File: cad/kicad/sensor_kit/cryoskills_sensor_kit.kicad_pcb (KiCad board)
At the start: 2 copper layers, 150 x 60 mm, 58 parts, among them J1 PWR_In, J10 QWIIC_I2C_2, J12 DS18B20, J13 Conn_01x02, J14 PT1000_RTD_WHEAT, J2 PWR_SENSE_Panel, J3 PWR_SENSE_Battery, J4 Conn_01x02, J5 Conn_01x02, J6 Conn_01x02, J7 PT1000_RTD_CC, J8 SPI_BREAKOUT, J9 QWIIC_I2C_1, SW1 SPDT Switch, U1 LM317_TO-220, U2 RFM96W, U3 INA3221, U4 LM334Z, U5 LM234Z-3

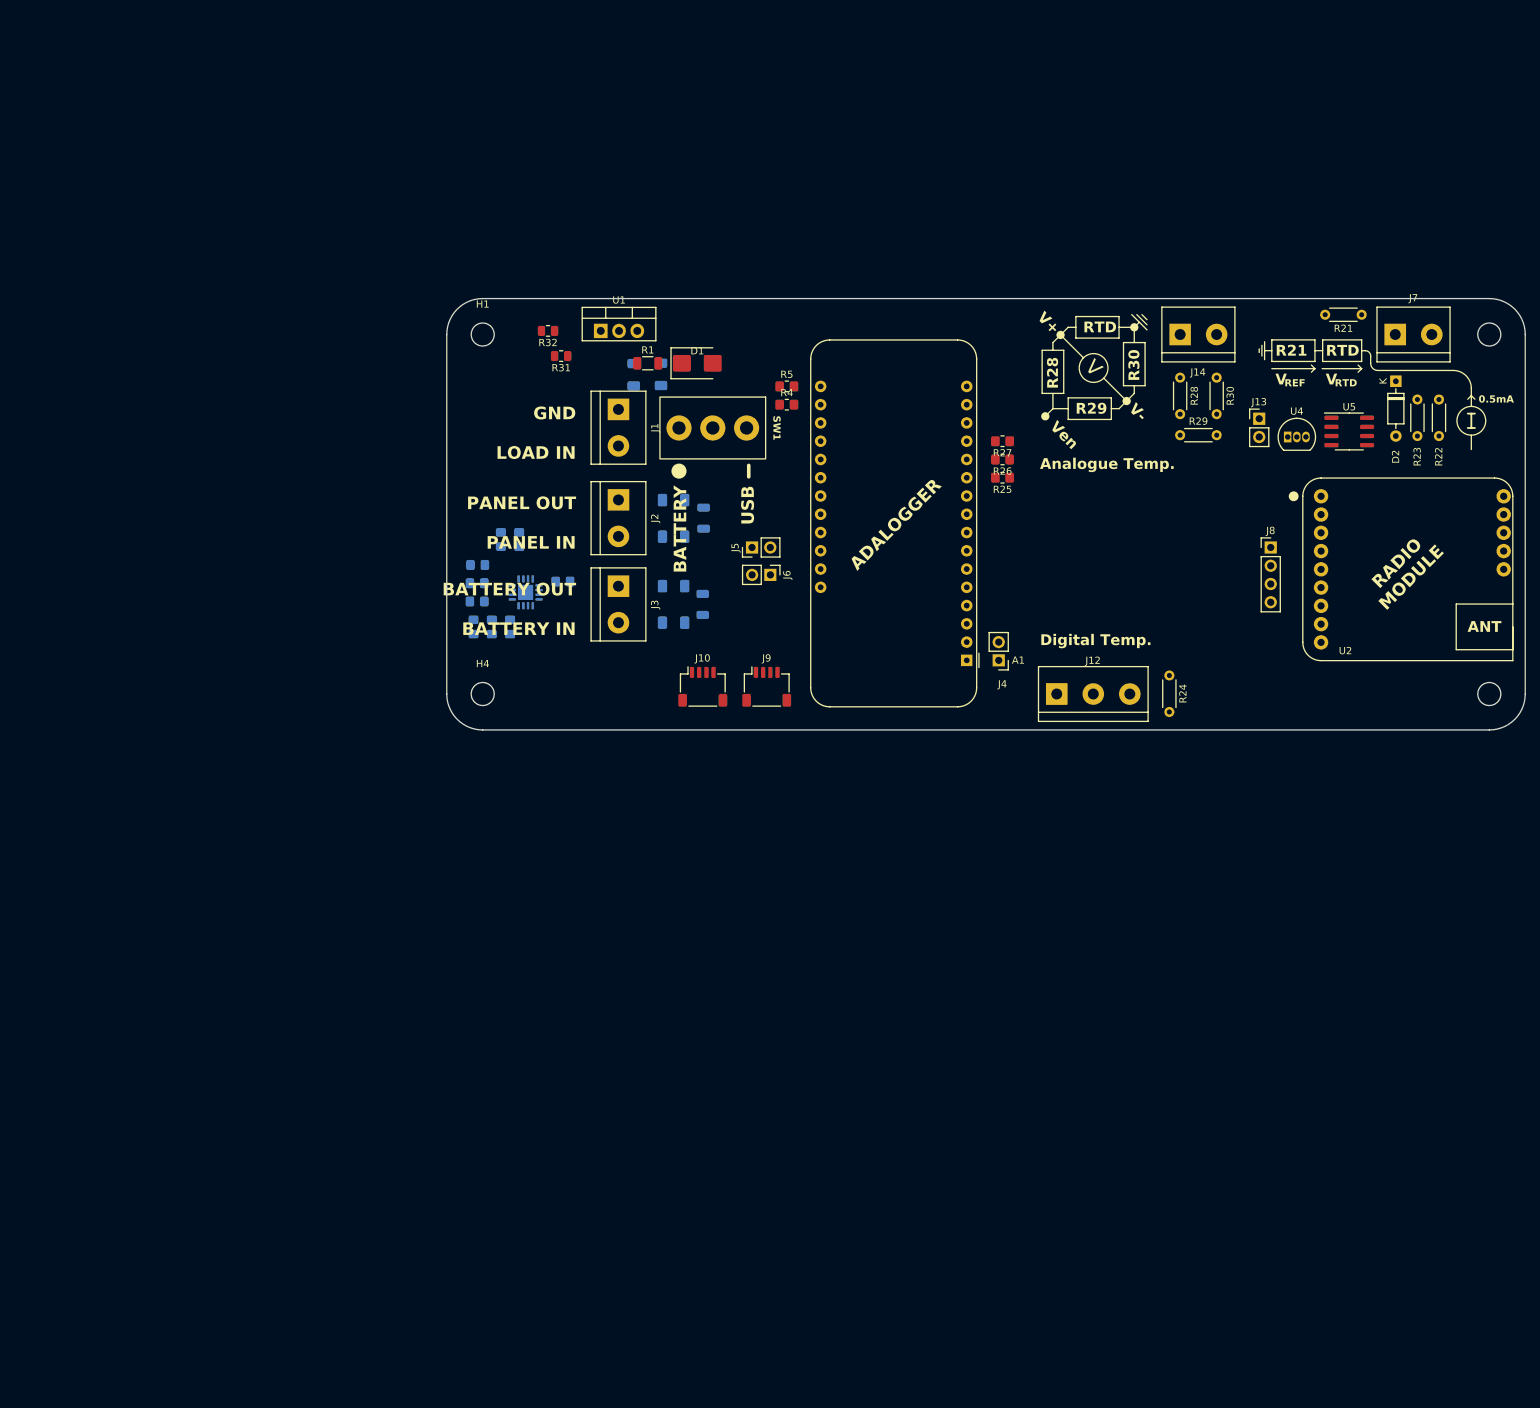
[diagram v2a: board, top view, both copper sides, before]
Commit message: revises sensor board to remove current source and reduce footprint
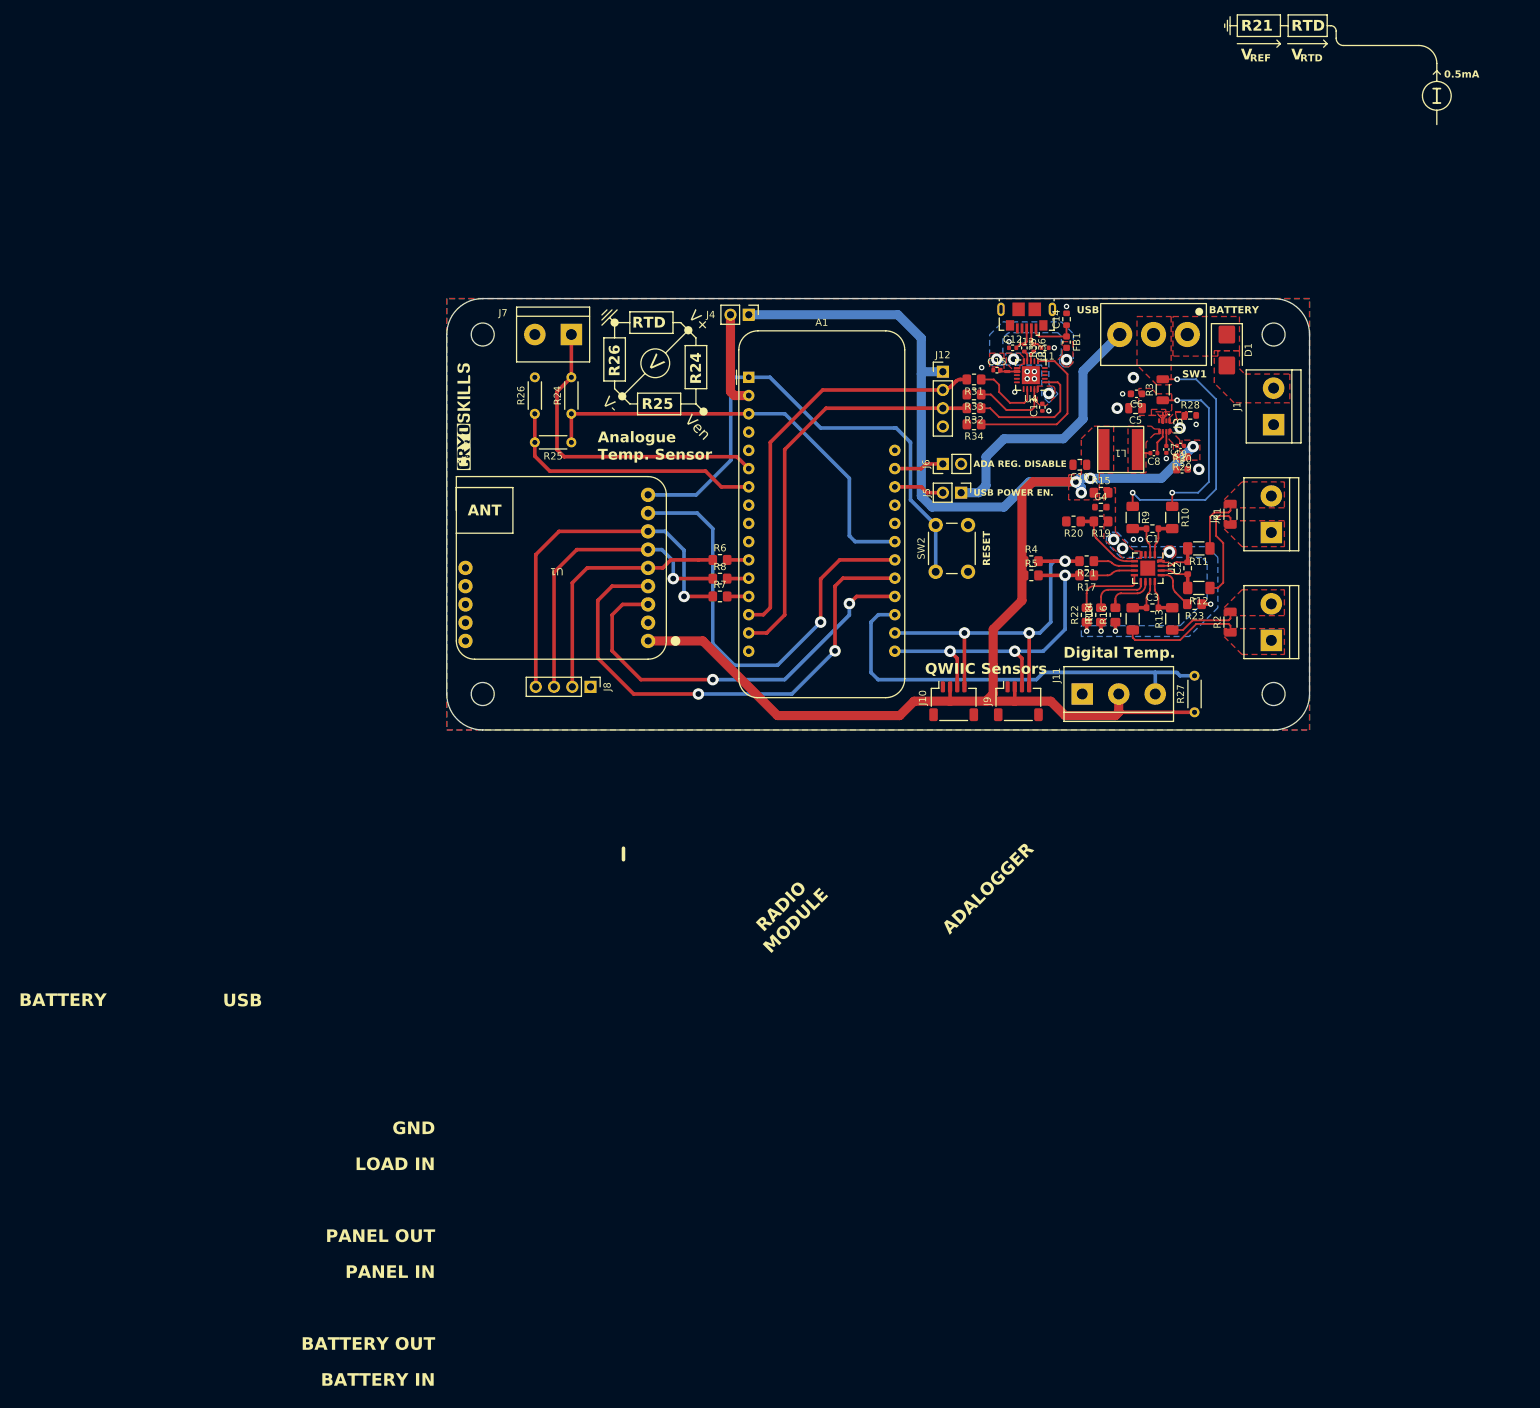
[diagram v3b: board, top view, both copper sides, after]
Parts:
- removed D2: 1N4149, Diode_THT:D_DO-35_SOD27_P7.62mm_Horizontal
- removed J14: PT1000_RTD_WHEAT, cryoskills_sensor_kit:TerminalBlock_Multicomp_5.08_2way_MP012059
- removed U5: LM234Z-3, Package_SO:SOIC-8_3.9x4.9mm_P1.27mm
- added C1: 0.1 uF, Resistor_SMD:R_0603_1608Metric, F.Cu at (156.7, 104.0)
- added C10: 100nF, Capacitor_SMD:C_0805_2012Metric, F.Cu at (146.6, 95.1)
- added C11: 47pF, Resistor_SMD:R_0402_1005Metric, F.Cu at (141.7, 78.8)
- added C12: 47pF, Resistor_SMD:R_0402_1005Metric, F.Cu at (137.2, 78.9)
- added C13: 100nF, Resistor_SMD:R_0402_1005Metric, F.Cu at (141.3, 87.1)
- added C14: 10nF, Resistor_SMD:R_0603_1608Metric, F.Cu at (144.7, 74.9)
- added C15: 100nF, Resistor_SMD:R_0402_1005Metric, F.Cu at (135.0, 82.0)
- added C2: 0.1 uF, Resistor_SMD:R_0603_1608Metric, F.Cu at (161.6, 109.5)
- added C3: 0.1 uF, Resistor_SMD:R_0603_1608Metric, F.Cu at (156.7, 115.0)
- added C4: 0.1 uF, Resistor_SMD:R_0603_1608Metric, F.Cu at (149.5, 101.0)
- added C5: 10uF, Capacitor_SMD:C_0805_2012Metric, F.Cu at (154.3, 87.2)
- added C6: 100nF, Capacitor_SMD:C_0603_1608Metric, F.Cu at (154.4, 85.2)
- added C7: 33nF, Capacitor_SMD:C_0402_1005Metric, F.Cu at (158.6, 93.0)
- added C8: 100nF, Capacitor_SMD:C_0402_1005Metric, F.Cu at (156.8, 93.5)
- added C9: 47pF, Capacitor_SMD:C_0402_1005Metric, F.Cu at (160.6, 92.5)
- added FB1: FerriteBead, Inductor_SMD:L_0603_1608Metric, F.Cu at (144.7, 78.1)
- added G***: LOGO, LOGO, F.Cu at (60.5, 88.5)
- added J11: DS18B20, cryoskills_sensor_kit:TerminalBlock_Multicomp_5.08_3way_MP012060, F.Cu at (146.9, 127.0)
- added L1: 2.7uH, cryoskills_sensor_kit:1255AY-2R7N#, F.Cu at (152.2, 93.0)
- added R33: 0R, Resistor_SMD:R_0805_2012Metric_Pad1.20x1.40mm_HandSolder, F.Cu at (131.8, 85.3)
- added R34: 0R, Resistor_SMD:R_0805_2012Metric_Pad1.20x1.40mm_HandSolder, F.Cu at (131.8, 89.5)
- added R35: 27R, Resistor_SMD:R_0402_1005Metric, F.Cu at (138.8, 78.9)
- added R36: 27R, Resistor_SMD:R_0402_1005Metric, F.Cu at (140.1, 78.8)
- added SW2: SW_Push, Button_Switch_THT:SW_PUSH_6mm, F.Cu at (126.5, 110.0)
- J12: value DS18B20 -> SERIAL_BREAKOUT; footprint cryoskills_sensor_kit:TerminalBlock_Multicomp_5.08_3way_MP012060 -> Connector_PinHeader_2.54mm:PinHeader_1x04_P2.54mm_Vertical
- J13: value Conn_01x02 -> USB_B; footprint Connector_PinHeader_2.54mm:PinHeader_1x02_P2.54mm_Vertical -> Connector_USB:USB_Micro-B_GCT_USB3076-30-A
- J4: value Conn_01x02 -> Adalogger_3V3
- J5: value Conn_01x02 -> Adalogger_VBUS
- J6: value Conn_01x02 -> Adalogger_RegulatorEN
- J7: value PT1000_RTD_CC -> PT1000_RTD_WHEAT
- R10, R11, R17, R2, R3, R9: moved to F.Cu
- R12, R14: value 0R -> 10 Ohm; footprint Resistor_SMD:R_0805_2012Metric_Pad1.20x1.40mm_HandSolder -> Resistor_SMD:R_1206_3216Metric_Pad1.30x1.75mm_HandSolder; moved to F.Cu
- R13: value 10k -> 10 Ohm; footprint Resistor_SMD:R_0805_2012Metric_Pad1.20x1.40mm_HandSolder -> Resistor_SMD:R_1206_3216Metric_Pad1.30x1.75mm_HandSolder; moved to F.Cu
- R15, R20: value 10k -> 0R; moved to F.Cu
- R16: value DNF -> 10k; moved to F.Cu
- R18: value 0R -> 10k; moved to F.Cu
- R19: value 10k -> DNF; moved to F.Cu
- R21: value 3k -> 0R; footprint Resistor_THT:R_Axial_DIN0204_L3.6mm_D1.6mm_P5.08mm_Horizontal -> Resistor_SMD:R_0805_2012Metric_Pad1.20x1.40mm_HandSolder
- R22: value 330R -> 10k; footprint Resistor_THT:R_Axial_DIN0204_L3.6mm_D1.6mm_P5.08mm_Horizontal -> Resistor_SMD:R_0805_2012Metric_Pad1.20x1.40mm_HandSolder
- R23: value 2.4k -> 10k; footprint Resistor_THT:R_Axial_DIN0204_L3.6mm_D1.6mm_P5.08mm_Horizontal -> Resistor_SMD:R_0805_2012Metric_Pad1.20x1.40mm_HandSolder
- R24: value 4.7k -> 3k3
- R25: value 0R -> 3k3; footprint Resistor_SMD:R_0805_2012Metric_Pad1.20x1.40mm_HandSolder -> Resistor_THT:R_Axial_DIN0204_L3.6mm_D1.6mm_P5.08mm_Horizontal
- R26: value 0R -> 1k; footprint Resistor_SMD:R_0805_2012Metric_Pad1.20x1.40mm_HandSolder -> Resistor_THT:R_Axial_DIN0204_L3.6mm_D1.6mm_P5.08mm_Horizontal
- R27: value 0R -> 4.7k; footprint Resistor_SMD:R_0805_2012Metric_Pad1.20x1.40mm_HandSolder -> Resistor_THT:R_Axial_DIN0204_L3.6mm_D1.6mm_P5.08mm_Horizontal
- R28: value 3k -> 15k; footprint Resistor_THT:R_Axial_DIN0204_L3.6mm_D1.6mm_P5.08mm_Horizontal -> Resistor_SMD:R_0603_1608Metric
- R29: value 3k -> 30.9k; footprint Resistor_THT:R_Axial_DIN0204_L3.6mm_D1.6mm_P5.08mm_Horizontal -> Capacitor_SMD:C_0603_1608Metric
- R30: value 1k -> 10k; footprint Resistor_THT:R_Axial_DIN0204_L3.6mm_D1.6mm_P5.08mm_Horizontal -> Capacitor_SMD:C_0603_1608Metric
- R31: value 1.2k -> 0R; footprint Resistor_SMD:R_0805_2012Metric -> Resistor_SMD:R_0805_2012Metric_Pad1.20x1.40mm_HandSolder
- R32: value 1.8k -> 0R; footprint Resistor_SMD:R_0805_2012Metric -> Resistor_SMD:R_0805_2012Metric_Pad1.20x1.40mm_HandSolder
- R6, R7, R8: value 10 Ohm -> 0R; footprint Resistor_SMD:R_1206_3216Metric_Pad1.30x1.75mm_HandSolder -> Resistor_SMD:R_0805_2012Metric_Pad1.20x1.40mm_HandSolder; moved to F.Cu
- U1: value LM317_TO-220 -> RFM96W; footprint Package_TO_SOT_THT:TO-220-3_Vertical -> cryoskills_sensor_kit:RFM96W
- U2: value RFM96W -> INA3221; footprint cryoskills_sensor_kit:RFM96W -> Package_DFN_QFN:Texas_RGV_S-PVQFN-N16_EP2.1x2.1mm
- U3: value INA3221 -> TPS62932DRLR; footprint Package_DFN_QFN:Texas_RGV_S-PVQFN-N16_EP2.1x2.1mm -> cryoskills_sensor_kit:TPS62932DRLR; moved to F.Cu
- U4: value LM334Z -> FT231XQ; footprint Package_TO_SOT_THT:TO-92_Inline -> Package_DFN_QFN:QFN-20-1EP_4x4mm_P0.5mm_EP2.5x2.5mm
- moved H3 148.7 mm to (63.5, 77.0)
- moved J7 114.6 mm to (75.8, 77.0), turned to 180 degrees
- moved H1 110.0 mm to (173.5, 77.0)
- moved J8 96.6 mm to (78.5, 126.0), turned to -90 degrees
- moved R12 96.0 mm to (163.1, 112.2), turned to 180 degrees
- moved U3 91.8 mm to (158.3, 89.7), turned to -90 degrees
- moved R13 91.5 mm to (159.4, 116.5), turned to 90 degrees
- moved R14 91.3 mm to (153.9, 116.5), turned to 90 degrees
- moved J1 91.1 mm to (173.5, 89.5), turned to 90 degrees
- moved J3 91.1 mm to (173.2, 119.5), turned to 90 degrees
- moved J2 90.9 mm to (173.2, 104.5), turned to 90 degrees
- moved R24 90.8 mm to (75.8, 88.0), turned to 90 degrees
- moved R19 86.9 mm to (149.5, 103.0)
- moved R18 86.8 mm to (149.5, 116.0), turned to 90 degrees
- moved R16 86.8 mm to (151.5, 116.0)
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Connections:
- net Net-(A1-3V3) renamed /VCC_3V3_Adalogger
- net Net-(A1-USB) renamed /VBUS_Adalogger
- A1 pad 21: /RADIO_CS -> /RADIO_IRQ
- A1 pad 22: /RADIO_IRQ -> /RADIO_CS
- A1 pad 23: /RTD_WHEAT_EN -> /ADC_REF+
- A1 pad 6: /ADC_RTD+ -> /ADC_RTDp
- A1 pad 7: /ADC_REF+ -> /ADC_RTDm
- D1 pad 1: /Isense_VCC_A -> Net-(D1-K)
- D1 pad 2: /V_IN -> /V_BAT
- J10 pad 3: /SCL -> /SDA
- J10 pad 4: /SDA -> /SCL
- J12 pad 1: GND -> /VCC_3V3
- J12 pad 2: /VCC_3V3 -> /UART_RXuC
- J12 pad 3: /DS18B20_DATA -> /UART_TXuC
- J13 pad 1: /VCC_3V3 -> Net-(J13-VBUS)
- J13 pad 2: /Sensors/CC_IN -> Net-(J13-D-)
- J7 pad 1: /ADC_RTD+ -> /ADC_RTDp
- J7 pad 2: /ADC_REF+ -> GND
- J9 pad 3: /SCL -> /SDA
- J9 pad 4: /SDA -> /SCL
- R1 pad 1: /Isense_VCC_B -> /Isense_Panel_B
- R1 pad 2: /Isense_VCC_A -> /Isense_Panel_A
- R10 pad 1: /Isense_Battery_A -> /Isense_VCC_B
- R10 pad 2: /Power Monitor/INA3221_IN+3 -> /Power Monitor/INA3221_INm3
- R11 pad 1: /Isense_Battery_B -> /Isense_Panel_A
- R11 pad 2: /Power Monitor/INA3221_IN-3 -> /Power Monitor/INA3221_INp2
- R12 pad 1: /VCC_3V3 -> /Isense_Panel_B
- R12 pad 2: /Power Monitor/VCC_INA3221 -> /Power Monitor/INA3221_INm2
- R13 pad 1: /Power Monitor/VCC_INA3221 -> /Isense_Battery_A
- R13 pad 2: unconnected-(R13-Pad2) -> /Power Monitor/INA3221_INp1
- R14 pad 1: Net-(U3-SDA) -> /Isense_Battery_B
- R14 pad 2: /SDA -> /Power Monitor/INA3221_INm1
- R15 pad 1: /Power Monitor/VCC_INA3221 -> /VCC_3V3
- R15 pad 2: unconnected-(R15-Pad2) -> /Power Monitor/VCC_INA3221
- R16 pad 2: /Power Monitor/INA3221_I2CAddress -> unconnected-(R16-Pad2)
- R17 pad 1: /Power Monitor/INA3221_I2CAddress -> Net-(U2-SDA)
- R17 pad 2: GND -> /SDA
- R18 pad 1: Net-(U3-SCL) -> /Power Monitor/VCC_INA3221
- R18 pad 2: /SCL -> unconnected-(R18-Pad2)
- R19 pad 2: unconnected-(R19-Pad2) -> /Power Monitor/INA3221_I2CAddress
- R2 pad 1: /Isense_Panel_B -> /Isense_Battery_B
- R2 pad 2: /Isense_Panel_A -> /Isense_Battery_A
- R20 pad 1: /Power Monitor/VCC_INA3221 -> /Power Monitor/INA3221_I2CAddress
- R20 pad 2: unconnected-(R20-Pad2) -> GND
- R21 pad 1: /ADC_REF+ -> Net-(U2-SCL)
- R21 pad 2: GND -> /SCL
- R22 pad 1: /Sensors/CC_ADJ -> /Power Monitor/VCC_INA3221
- R22 pad 2: /Sensors/CC_OUT -> unconnected-(R22-Pad2)
- R23 pad 1: /Sensors/CC_ADJ -> /Power Monitor/VCC_INA3221
- R23 pad 2: /ADC_RTD+ -> unconnected-(R23-Pad2)
- R24 pad 1: /VCC_3V3 -> /ADC_REF+
- R24 pad 2: /DS18B20_DATA -> /ADC_RTDp
- R25 pad 1: /SCK -> /ADC_REF+
- R25 pad 2: Net-(A1-SCK/D24) -> /ADC_RTDm
- R26 pad 1: /MOSI -> /ADC_RTDm
- R26 pad 2: Net-(A1-MOSI/D23) -> GND
- R27 pad 1: /MISO -> /VCC_3V3
- R27 pad 2: Net-(A1-MISO/D22) -> /DS18B20_DATA
- R28 pad 1: /ADC_REF+ -> Net-(U3-RT)
- R28 pad 2: /ADC_RTD+ -> GND
- R29 pad 1: /ADC_REF+ -> /VCC_3V3
- R29 pad 2: /ADC_REF+ -> Net-(U3-FB)
- R3 pad 1: /Isense_Battery_B -> /Isense_VCC_B
- R3 pad 2: /Isense_Battery_A -> /Isense_VCC_A
- R30 pad 1: /ADC_REF+ -> Net-(U3-FB)
- R31 pad 1: /VCC_3V3 -> Net-(U4-TXD)
- R31 pad 2: Net-(U1-ADJ) -> /UART_RXuC
- R32 pad 1: Net-(U1-ADJ) -> Net-(U4-RXD)
- R32 pad 2: GND -> /UART_TXuC
- R6 pad 1: /Isense_VCC_A -> /SCK
- R6 pad 2: /Power Monitor/INA3221_IN+1 -> Net-(A1-SCK/D24)
- R7 pad 1: /Isense_VCC_B -> /MISO
- R7 pad 2: /Power Monitor/INA3221_IN-1 -> Net-(A1-MISO/D22)
- R8 pad 1: /Isense_Panel_A -> /MOSI
- R8 pad 2: /Power Monitor/INA3221_IN+2 -> Net-(A1-MOSI/D23)
- R9 pad 1: /Isense_Panel_B -> /Isense_VCC_A
- R9 pad 2: /Power Monitor/INA3221_IN-2 -> /Power Monitor/INA3221_INp3
- SW1 pad 1: /V_BAT -> Net-(D1-K)
- SW1 pad 2: /V_IN -> /Isense_VCC_A
- U1 pad 1: Net-(U1-ADJ) -> /VCC_3V3
- U1 pad 2: /VCC_3V3 -> GND
- U1 pad 3: /Isense_VCC_B -> /RADIO_EN
- U2 pad 1: /VCC_3V3 -> /Power Monitor/INA3221_INm3
- U2 pad 10: unconnected-(U2-G5-Pad10) -> unconnected-(R16-Pad2)
- U2 pad 11: unconnected-(U2-G4-Pad11) -> /Power Monitor/INA3221_INm1
- U2 pad 12: unconnected-(U2-G3-Pad12) -> /Power Monitor/INA3221_INp1
- U2 pad 13: unconnected-(U2-G2-Pad13) -> unconnected-(R23-Pad2)
- U2 pad 14: unconnected-(U2-G1-Pad14) -> /Power Monitor/INA3221_INm2
- U2 pad 2: GND -> /Power Monitor/INA3221_INp3
- U2 pad 3: /RADIO_EN -> GND
- U2 pad 4: /RADIO_IRQ -> /Power Monitor/VCC_INA3221
- U2 pad 5: /SCK -> /Power Monitor/INA3221_I2CAddress
- U2 pad 6: /MOSI -> Net-(U2-SCL)
- U2 pad 7: /MISO -> Net-(U2-SDA)
- U2 pad 8: /RADIO_CS -> unconnected-(R22-Pad2)
- U2 pad 9: /~{RESET} -> unconnected-(R18-Pad2)
- U3 pad 1: /Power Monitor/INA3221_IN-3 -> Net-(U3-RT)
- U3 pad 2: /Power Monitor/INA3221_IN+3 -> unconnected-(U3-EN-Pad2)
- U3 pad 3: GND -> /Isense_VCC_B
- U3 pad 4: /Power Monitor/VCC_INA3221 -> GND
- U3 pad 5: /Power Monitor/INA3221_I2CAddress -> Net-(U3-SW)
- U3 pad 6: Net-(U3-SCL) -> Net-(U3-BST)
- U3 pad 7: Net-(U3-SDA) -> Net-(U3-SS)
- U3 pad 8: unconnected-(R19-Pad2) -> Net-(U3-FB)
- U4 pad 1: /Sensors/CC_IN -> Net-(U4-RXD)
- U4 pad 2: /Sensors/CC_ADJ -> unconnected-(U4-~{RI}-Pad2)
- U4 pad 3: /Sensors/CC_OUT -> GND
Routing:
- net /VCC_3V3: track 0.00 -> 224.3 mm, vias 0 -> 4
- net /~{RESET}: track 0.00 -> 73.1 mm
- net /RADIO_IRQ: track 0.00 -> 71.2 mm, vias 0 -> 2
- net /RADIO_CS: track 0.00 -> 62.0 mm, vias 0 -> 1
- net /ADC_REF+: track 0.00 -> 60.5 mm
- net /DS18B20_DATA: track 0.00 -> 59.8 mm
- net /RADIO_EN: track 0.00 -> 57.3 mm, vias 0 -> 2
- net /UART_RXuC: track 0.00 -> 57.2 mm
- net /UART_TXuC: track 0.00 -> 56.8 mm
- net /SCL: track 0.00 -> 53.3 mm, vias 0 -> 3
- net /MISO: track 0.00 -> 51.9 mm, vias 0 -> 1
- net /SDA: track 0.00 -> 48.9 mm, vias 0 -> 3
- net /ADC_RTDp: track 0.00 -> 44.6 mm
- net /MOSI: track 0.00 -> 42.4 mm, vias 0 -> 1
- net /V_BUS: track 0.00 -> 37.4 mm
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- added copper zone on F.Cu, net /Isense_Battery_A
- added copper zone on F.Cu, net /Isense_Battery_B
- added copper zone on F.Cu, net /Isense_Panel_A
- added copper zone on F.Cu, net /Isense_Panel_B
- added copper zone on F.Cu, net /Isense_VCC_A
- added copper zone on F.Cu, net /Isense_VCC_B
- added copper zone on B.Cu, net /Power Monitor/VCC_INA3221
- added copper zone on F.Cu, net /Power Monitor/VCC_INA3221
- added copper zone on F.Cu, net /VCC_3V3
- added copper zone on F.Cu, net /V_BAT
- added copper zone on B.Cu, net GND
- added copper zone on F.Cu, net GND
- added copper zone on F.Cu, net Net-(D1-K)
- added copper zone on F.Cu, net Net-(U3-FB)
- added copper zone on F.Cu, net Net-(U3-RT)
- added copper zone on F.Cu, net Net-(U3-SW)
- added copper zone on B.Cu, net Net-(U4-3V3OUT)
- added copper zone on F.Cu, net Net-(U4-3V3OUT)
- added copper zone on B.Cu, net Net-(U4-VCC)
- added copper zone on F.Cu, net Net-(U4-VCC)
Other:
- board size 150 x 60 mm -> 120 x 60 mm
- board text added: "ADA REG. DISABLE"
- board text added: "Analogue Temp. Sensor"
- board text added: "QWIIC Sensors"
- board text added: "R24"
- board text added: "R25"
- board text added: "R26"
- board text added: "RESET"
- board text added: "USB POWER EN."
- board text removed: "Analogue Temp."
- board text removed: "R28"
- board text removed: "R29"
- board text removed: "R30"
